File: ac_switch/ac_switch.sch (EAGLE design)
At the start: 20 parts, among them IC1 TINY85, T1 BC337, X2 SSW-102-02-S-S-RA

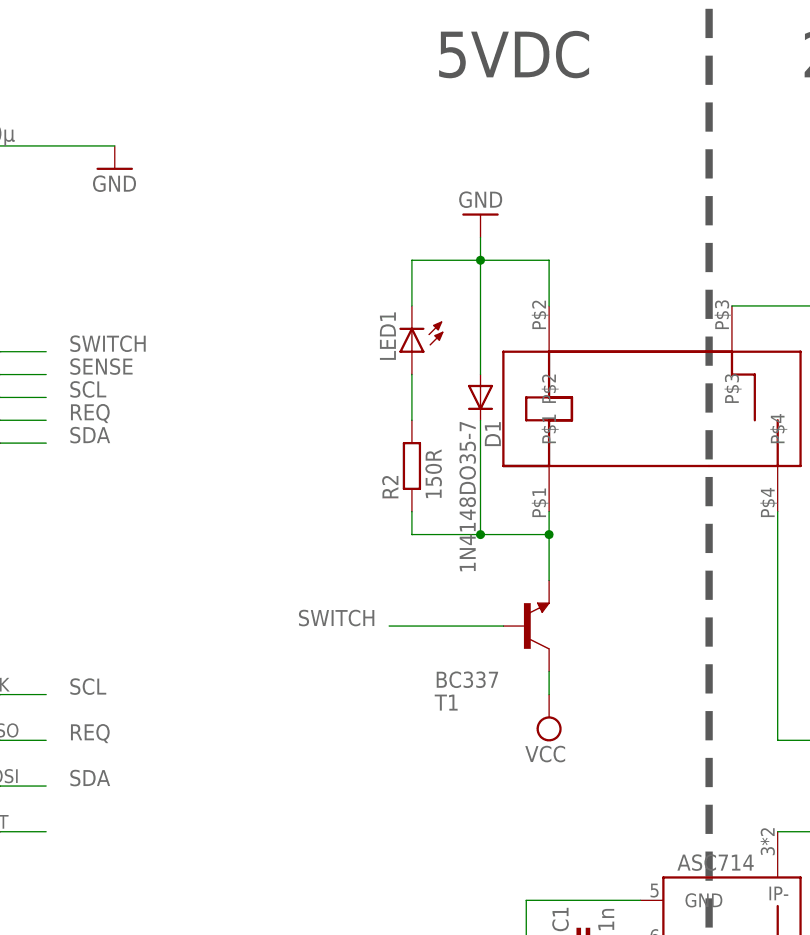
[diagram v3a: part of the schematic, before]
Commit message: * Transistor in Emitterschaltung (dann mit Vorwiderstand)
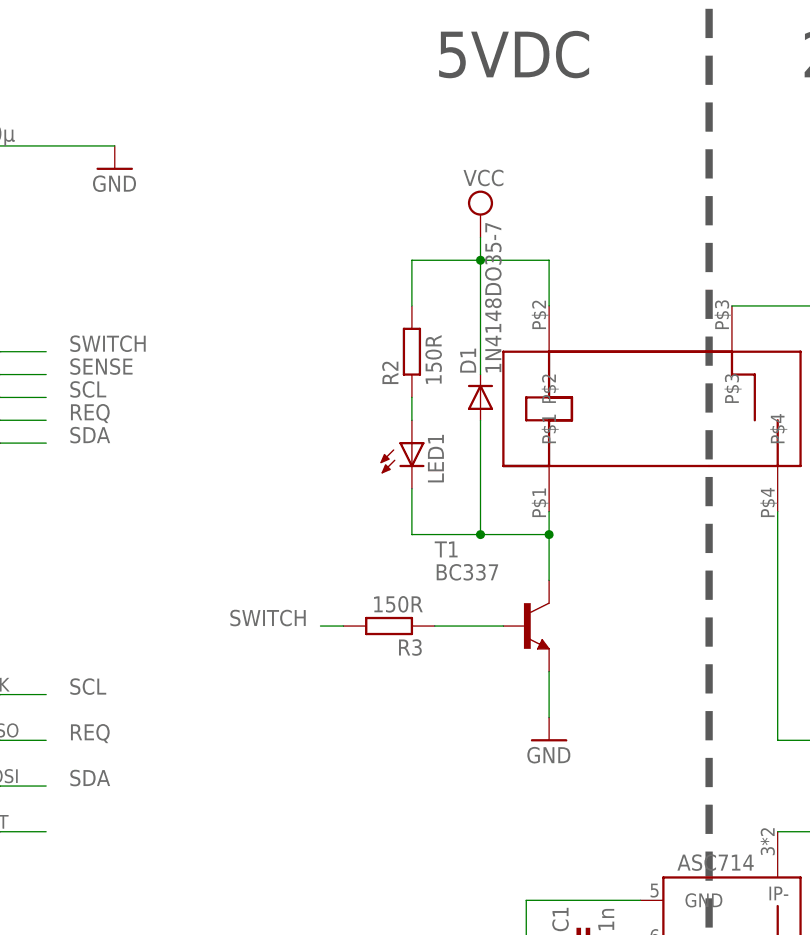
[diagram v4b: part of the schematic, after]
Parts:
- added R3: 150R, resistor:R-EU_0204/7
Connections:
- new net N$4: LED1.A, R2.1
- net GND: now also T1.E; no longer D1.A, LED1.C, U$1.P$2
- net N$1: now also D1.A, LED1.C, T1.C; no longer D1.C, R2.1, T1.E
- net N$5: now also R3.1, T1.B; no longer LED1.A, R2.2
- net SWITCH: now also R3.2; no longer T1.B
- net VCC: now also D1.C, R2.2, U$1.P$2; no longer T1.C
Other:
- moved on the sheet: D1, LED1, R2, T1
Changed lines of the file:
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@@
 <part name="U$5" library="n39" deviceset="I3C_PORT" device=""/>
 <part name="X2" library="con-samtec" deviceset="SSW-102-02-S-S" device="-RA"/>
+<part name="R3" library="resistor" deviceset="R-EU_" device="0204/7" value="150R"/>
 </parts>
 <sheets>
@@
 <instance part="U$1" gate="G$1" x="48.26" y="35.56"/>
 <instance part="U$2" gate="ACS714" x="73.66" y="-22.86" rot="R180"/>
-<instance part="D1" gate="G$1" x="45.72" y="43.18" rot="R270"/>
+<instance part="D1" gate="G$1" x="45.72" y="43.18" rot="R90"/>
 <instance part="SUPPLY1" gate="G$1" x="58.42" y="-35.56" rot="R180"/>
-<instance part="T1" gate="G$1" x="50.8" y="17.78" rot="MR180"/>
-<instance part="SUPPLY2" gate="G$1" x="53.34" y="7.62" rot="R180"/>
-<instance part="GND2" gate="1" x="45.72" y="63.5" rot="R180"/>
+<instance part="T1" gate="G$1" x="50.8" y="17.78"/>
+<instance part="SUPPLY2" gate="G$1" x="45.72" y="63.5"/>
+<instance part="GND2" gate="1" x="53.34" y="5.08"/>
 <instance part="C1" gate="G$1" x="55.88" y="-17.78" rot="R90"/>
 <instance part="C2" gate="G$1" x="53.34" y="-27.94" rot="R90"/>
@@
 <instance part="C3" gate="G$1" x="-66.04" y="38.1" rot="R180"/>
 <instance part="R1" gate="G$1" x="-55.88" y="48.26"/>
-<instance part="LED1" gate="G$1" x="38.1" y="48.26" rot="R180"/>
-<instance part="R2" gate="G$1" x="38.1" y="35.56" rot="R90"/>
+<instance part="LED1" gate="G$1" x="38.1" y="38.1"/>
+<instance part="R2" gate="G$1" x="38.1" y="48.26" rot="R90"/>
 <instance part="U$3" gate="G$1" x="-60.96" y="2.54"/>
 <instance part="U$4" gate="G$1" x="-10.16" y="2.54"/>
@@
 <instance part="X2" gate="-1" x="129.54" y="20.32" rot="R180"/>
 <instance part="X2" gate="-2" x="129.54" y="22.86" rot="R180"/>
+<instance part="R3" gate="G$1" x="35.56" y="17.78" rot="R180"/>
 </instances>
 <busses>
@@
 <pinref part="U$1" gate="G$1" pin="P$1"/>
 <wire x1="53.34" y1="30.48" x2="53.34" y2="27.94" width="0.1524" layer="91"/>
+<wire x1="38.1" y1="27.94" x2="45.72" y2="27.94" width="0.1524" layer="91"/>
+<pinref part="T1" gate="G$1" pin="C"/>
 <wire x1="45.72" y1="27.94" x2="53.34" y2="27.94" width="0.1524" layer="91"/>
-<pinref part="D1" gate="G$1" pin="C"/>
+<wire x1="53.34" y1="22.86" x2="53.34" y2="27.94" width="0.1524" layer="91"/>
+<junction x="53.34" y="27.94"/>
+<pinref part="LED1" gate="G$1" pin="C"/>
+<wire x1="38.1" y1="33.02" x2="38.1" y2="27.94" width="0.1524" layer="91"/>
+<pinref part="D1" gate="G$1" pin="A"/>
 <wire x1="45.72" y1="40.64" x2="45.72" y2="27.94" width="0.1524" layer="91"/>
-<pinref part="T1" gate="G$1" pin="E"/>
-<wire x1="53.34" y1="27.94" x2="53.34" y2="22.86" width="0.1524" layer="91"/>
-<junction x="53.34" y="27.94"/>
-<pinref part="R2" gate="G$1" pin="1"/>
-<wire x1="38.1" y1="30.48" x2="38.1" y2="27.94" width="0.1524" layer="91"/>
-<wire x1="38.1" y1="27.94" x2="45.72" y2="27.94" width="0.1524" layer="91"/>
 <junction x="45.72" y="27.94"/>
 </segment>
@@
 </segment>
 <segment>
-<pinref part="T1" gate="G$1" pin="C"/>
-<pinref part="SUPPLY2" gate="G$1" pin="VCC"/>
-<wire x1="53.34" y1="12.7" x2="53.34" y2="10.16" width="0.1524" layer="91"/>
-</segment>
-<segment>
 <pinref part="SUPPLY4" gate="G$1" pin="VCC"/>
 <pinref part="C4" gate="G$1" pin="+"/>
 <wire x1="-22.86" y1="78.74" x2="-12.7" y2="78.74" width="0.1524" layer="91"/>
 </segment>
+<segment>
+<pinref part="U$1" gate="G$1" pin="P$2"/>
+<wire x1="53.34" y1="58.42" x2="53.34" y2="53.34" width="0.1524" layer="91"/>
+<wire x1="53.34" y1="58.42" x2="45.72" y2="58.42" width="0.1524" layer="91"/>
+<pinref part="SUPPLY2" gate="G$1" pin="VCC"/>
+<wire x1="45.72" y1="58.42" x2="38.1" y2="58.42" width="0.1524" layer="91"/>
+<wire x1="45.72" y1="60.96" x2="45.72" y2="58.42" width="0.1524" layer="91"/>
+<junction x="45.72" y="58.42"/>
+<pinref part="R2" gate="G$1" pin="2"/>
+<wire x1="38.1" y1="58.42" x2="38.1" y2="53.34" width="0.1524" layer="91"/>
+<pinref part="D1" gate="G$1" pin="C"/>
+<wire x1="45.72" y1="58.42" x2="45.72" y2="45.72" width="0.1524" layer="91"/>
+</segment>
 </net>
 <net name="GND" class="0">
-<segment>
-<pinref part="U$1" gate="G$1" pin="P$2"/>
-<wire x1="45.72" y1="58.42" x2="53.34" y2="58.42" width="0.1524" layer="91"/>
-<wire x1="53.34" y1="58.42" x2="53.34" y2="53.34" width="0.1524" layer="91"/>
-<pinref part="GND2" gate="1" pin="GND"/>
-<wire x1="45.72" y1="60.96" x2="45.72" y2="58.42" width="0.1524" layer="91"/>
-<pinref part="D1" gate="G$1" pin="A"/>
-<wire x1="45.72" y1="58.42" x2="45.72" y2="45.72" width="0.1524" layer="91"/>
-<junction x="45.72" y="58.42"/>
-<pinref part="LED1" gate="G$1" pin="C"/>
-<wire x1="45.72" y1="58.42" x2="38.1" y2="58.42" width="0.1524" layer="91"/>
-<wire x1="38.1" y1="58.42" x2="38.1" y2="53.34" width="0.1524" layer="91"/>
-</segment>
 <segment>
 <pinref part="IC1" gate="G$1" pin="GND"/>
@@
 <wire x1="-12.7" y1="71.12" x2="5.08" y2="71.12" width="0.1524" layer="91"/>
 </segment>
+<segment>
+<pinref part="GND2" gate="1" pin="GND"/>
+<pinref part="T1" gate="G$1" pin="E"/>
+<wire x1="53.34" y1="7.62" x2="53.34" y2="12.7" width="0.1524" layer="91"/>
+</segment>
 </net>
 <net name="N$2" class="0">
@@
 <net name="SWITCH" class="0">
 <segment>
-<pinref part="T1" gate="G$1" pin="B"/>
-<wire x1="48.26" y1="17.78" x2="35.56" y2="17.78" width="0.1524" layer="91"/>
-<label x="25.4" y="17.78" size="1.778" layer="95"/>
-</segment>
-<segment>
 <pinref part="IC1" gate="G$1" pin="PB4"/>
 <wire x1="-7.62" y1="48.26" x2="-2.54" y2="48.26" width="0.1524" layer="91"/>
 <label x="0" y="48.26" size="1.778" layer="95"/>
+</segment>
+<segment>
+<pinref part="R3" gate="G$1" pin="2"/>
+<wire x1="30.48" y1="17.78" x2="27.94" y2="17.78" width="0.1524" layer="91"/>
+<label x="17.78" y="17.78" size="1.778" layer="95"/>
 </segment>
 </net>
@@
 <pinref part="U$4" gate="G$1" pin="RST"/>
 <wire x1="-7.62" y1="-5.08" x2="-2.54" y2="-5.08" width="0.1524" layer="91"/>
-</segment>
-</net>
-<net name="N$5" class="0">
-<segment>
-<pinref part="LED1" gate="G$1" pin="A"/>
-<pinref part="R2" gate="G$1" pin="2"/>
-<wire x1="38.1" y1="45.72" x2="38.1" y2="40.64" width="0.1524" layer="91"/>
 </segment>
 </net>
@@
 </segment>
 </net>
+<net name="N$4" class="0">
+<segment>
+<pinref part="R2" gate="G$1" pin="1"/>
+<pinref part="LED1" gate="G$1" pin="A"/>
+<wire x1="38.1" y1="43.18" x2="38.1" y2="40.64" width="0.1524" layer="91"/>
+</segment>
+</net>
+<net name="N$5" class="0">
+<segment>
+<pinref part="T1" gate="G$1" pin="B"/>
+<pinref part="R3" gate="G$1" pin="1"/>
+<wire x1="48.26" y1="17.78" x2="40.64" y2="17.78" width="0.1524" layer="91"/>
+</segment>
+</net>

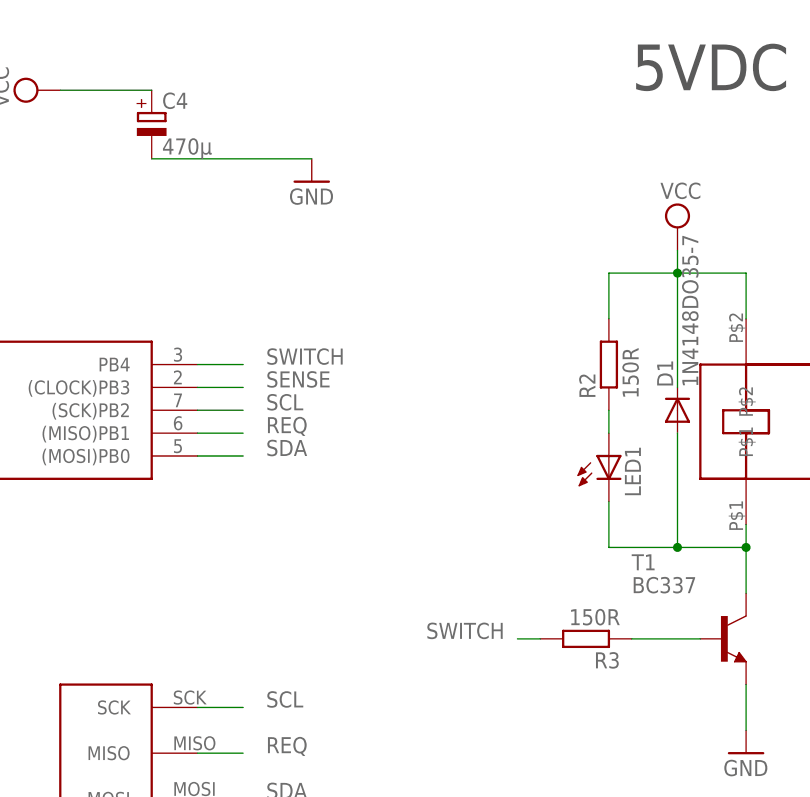
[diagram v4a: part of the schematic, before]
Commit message: * Werte für Widerstände und Kondensator (inkl. Package) angepasst * fine-tuning am PCB-Layout
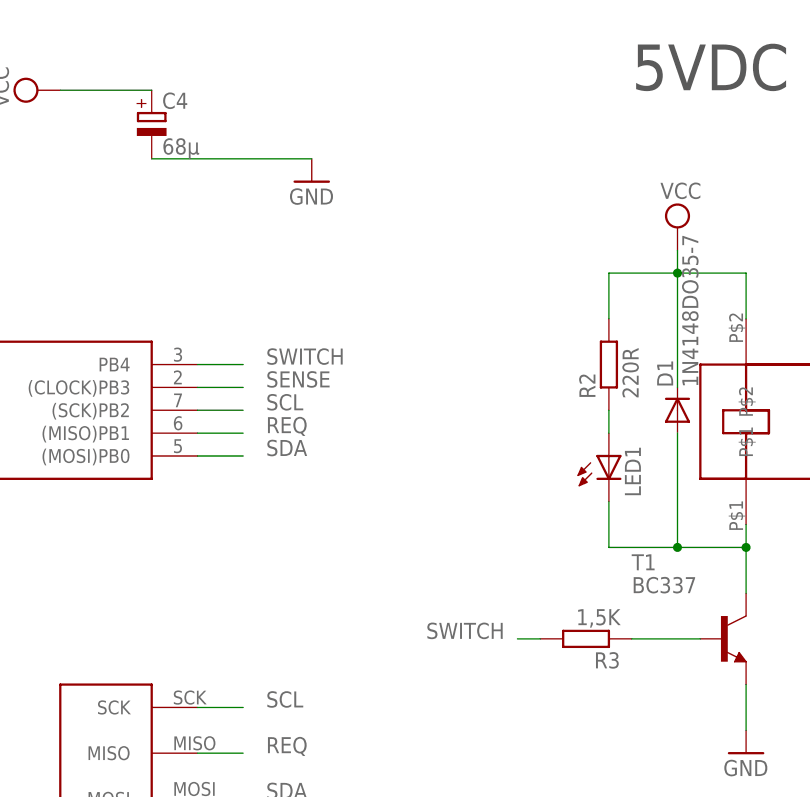
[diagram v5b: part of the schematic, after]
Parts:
- C4: value 470µ -> 68µ; device resistor:CPOL-EUE2.5-7 -> resistor:CPOL-EUE3.5-8
- R2: value 150R -> 220R
- R3: value 150R -> 1,5K
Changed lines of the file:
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@@
 <grid distance="0.1" unitdist="inch" unit="inch" style="lines" multiple="1" display="no" altdistance="0.01" altunitdist="inch" altunit="inch"/>
 <layers>
-<layer number="1" name="Top" color="4" fill="1" visible="no" active="no"/>
-<layer number="16" name="Bottom" color="1" fill="1" visible="no" active="no"/>
-<layer number="17" name="Pads" color="2" fill="1" visible="no" active="no"/>
-<layer number="18" name="Vias" color="2" fill="1" visible="no" active="no"/>
-<layer number="19" name="Unrouted" color="6" fill="1" visible="no" active="no"/>
-<layer number="20" name="Dimension" color="15" fill="1" visible="no" active="no"/>
-<layer number="21" name="tPlace" color="7" fill="1" visible="no" active="no"/>
-<layer number="22" name="bPlace" color="7" fill="1" visible="no" active="no"/>
-<layer number="23" name="tOrigins" color="15" fill="1" visible="no" active="no"/>
-<layer number="24" name="bOrigins" color="15" fill="1" visible="no" active="no"/>
-<layer number="25" name="tNames" color="7" fill="1" visible="no" active="no"/>
-<layer number="26" name="bNames" color="7" fill="1" visible="no" active="no"/>
-<layer number="27" name="tValues" color="7" fill="1" visible="no" active="no"/>
-<layer number="28" name="bValues" color="7" fill="1" visible="no" active="no"/>
+<layer number="1" name="Top" color="4" fill="1" visible="yes" active="no"/>
+<layer number="16" name="Bottom" color="1" fill="1" visible="yes" active="no"/>
+<layer number="17" name="Pads" color="2" fill="1" visible="yes" active="no"/>
+<layer number="18" name="Vias" color="2" fill="1" visible="yes" active="no"/>
+<layer number="19" name="Unrouted" color="6" fill="1" visible="yes" active="no"/>
+<layer number="20" name="Dimension" color="15" fill="1" visible="yes" active="no"/>
+<layer number="21" name="tPlace" color="7" fill="1" visible="yes" active="no"/>
+<layer number="22" name="bPlace" color="7" fill="1" visible="yes" active="no"/>
+<layer number="23" name="tOrigins" color="15" fill="1" visible="yes" active="no"/>
+<layer number="24" name="bOrigins" color="15" fill="1" visible="yes" active="no"/>
+<layer number="25" name="tNames" color="7" fill="1" visible="yes" active="no"/>
+<layer number="26" name="bNames" color="7" fill="1" visible="yes" active="no"/>
+<layer number="27" name="tValues" color="7" fill="1" visible="yes" active="no"/>
+<layer number="28" name="bValues" color="7" fill="1" visible="yes" active="no"/>
 <layer number="29" name="tStop" color="7" fill="3" visible="no" active="no"/>
 <layer number="30" name="bStop" color="7" fill="6" visible="no" active="no"/>
@@
 <layer number="35" name="tGlue" color="7" fill="4" visible="no" active="no"/>
 <layer number="36" name="bGlue" color="7" fill="5" visible="no" active="no"/>
-<layer number="37" name="tTest" color="7" fill="1" visible="no" active="no"/>
-<layer number="38" name="bTest" color="7" fill="1" visible="no" active="no"/>
+<layer number="37" name="tTest" color="7" fill="1" visible="yes" active="no"/>
+<layer number="38" name="bTest" color="7" fill="1" visible="yes" active="no"/>
 <layer number="39" name="tKeepout" color="4" fill="11" visible="no" active="no"/>
 <layer number="40" name="bKeepout" color="1" fill="11" visible="no" active="no"/>
@@
 <layer number="44" name="Drills" color="7" fill="1" visible="no" active="no"/>
 <layer number="45" name="Holes" color="7" fill="1" visible="no" active="no"/>
-<layer number="46" name="Milling" color="3" fill="1" visible="no" active="no"/>
-<layer number="47" name="Measures" color="7" fill="1" visible="no" active="no"/>
-<layer number="48" name="Document" color="7" fill="1" visible="no" active="no"/>
-<layer number="49" name="Reference" color="7" fill="1" visible="no" active="no"/>
-<layer number="51" name="tDocu" color="7" fill="1" visible="no" active="no"/>
-<layer number="52" name="bDocu" color="7" fill="1" visible="no" active="no"/>
+<layer number="46" name="Milling" color="3" fill="1" visible="yes" active="no"/>
+<layer number="47" name="Measures" color="7" fill="1" visible="yes" active="no"/>
+<layer number="48" name="Document" color="7" fill="1" visible="yes" active="no"/>
+<layer number="49" name="Reference" color="7" fill="1" visible="yes" active="no"/>
+<layer number="51" name="tDocu" color="7" fill="1" visible="yes" active="no"/>
+<layer number="52" name="bDocu" color="7" fill="1" visible="yes" active="no"/>
 <layer number="91" name="Nets" color="2" fill="1" visible="yes" active="yes"/>
 <layer number="92" name="Busses" color="1" fill="1" visible="yes" active="yes"/>
@@
 <part name="R1" library="resistor" deviceset="R-EU_" device="0207/10" value="10K"/>
 <part name="LED1" library="led" deviceset="LED" device="5MM"/>
-<part name="R2" library="resistor" deviceset="R-EU_" device="0204/7" value="150R"/>
+<part name="R2" library="resistor" deviceset="R-EU_" device="0204/7" value="220R"/>
 <part name="U$3" library="n39" deviceset="I3C_PORT" device=""/>
 <part name="U$4" library="n39" deviceset="AVR_ISP" device=""/>
@@
 <part name="GND4" library="supply1" deviceset="GND" device=""/>
 <part name="SUPPLY4" library="supply2" deviceset="VCC" device=""/>
-<part name="C4" library="resistor" deviceset="CPOL-EU" device="E2.5-7" value="470µ"/>
+<part name="C4" library="resistor" deviceset="CPOL-EU" device="E3.5-8" value="68µ"/>
 <part name="U$5" library="n39" deviceset="I3C_PORT" device=""/>
 <part name="X2" library="con-samtec" deviceset="SSW-102-02-S-S" device="-RA"/>
-<part name="R3" library="resistor" deviceset="R-EU_" device="0204/7" value="150R"/>
+<part name="R3" library="resistor" deviceset="R-EU_" device="0204/7" value="1,5K"/>
 </parts>
 <sheets>
